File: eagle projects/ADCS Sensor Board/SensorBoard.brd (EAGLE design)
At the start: 91 x 91 mm, 96 parts, among them J1 HDR_10_EZFET_DEBUGGER, J2 MTI-1_8428-11B1-RK-TP, Q1 BC850SMD, Q2 IRF7507TRPBF, U1 MSP430F5529IPN, U2 LMV321, U3 ADS7841E_2K5, U4 LMV321, U5 LMV321, Y1 32.768kHz, Y2 CSTCR4M00G15L99

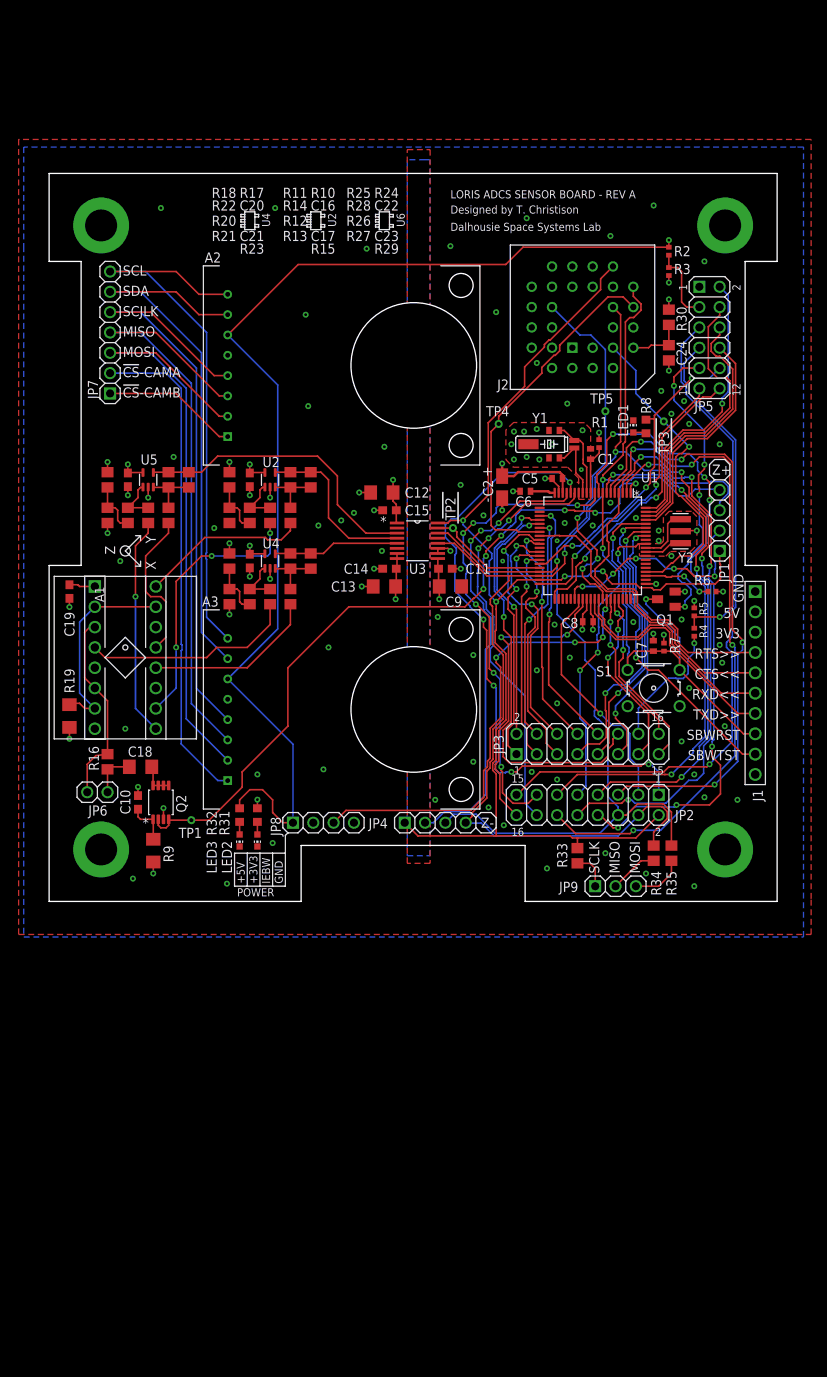
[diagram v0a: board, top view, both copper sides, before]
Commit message: Replaced obsolete transistor Q2
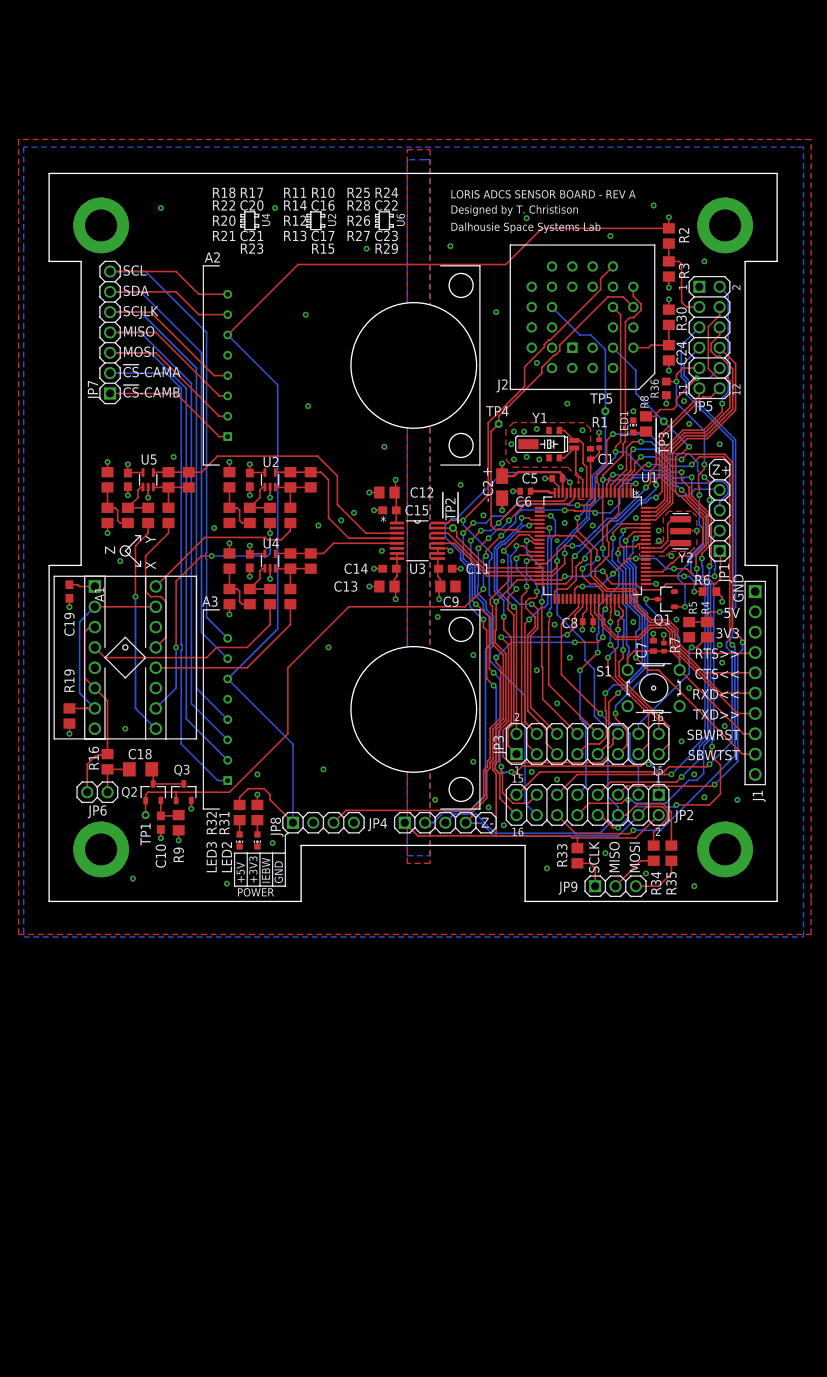
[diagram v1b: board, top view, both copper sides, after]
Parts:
- added Q3: IRLML2246TRPBF, my_library:SOT23-3P95_237X112L25X40N_MICRO3
- added R36: 10k, rcl:R0603
- C12, C13, C9: device resistor:C1206 -> rcl:C0805
- Q1: value BC850SMD -> PMV16XN; device transistor-npn:SOT23-BEC -> my_library:SOT23-3P95_230X110L20X43N_PMV16XN
- Q2: value IRF7507TRPBF -> IRLML6246TRPBF; device my_library:SOP8P65_300X490X111L53X30N -> my_library:SOT23-3P95_237X112L25X40N_MICRO3
- R19, R9: device resistor:R1206 -> rcl:R0805
- R2, R3, R4, R5: device rcl:R0402 -> rcl:R0805
- R31, R32, R8: device rcl:R0603 -> rcl:R0805
- R6: device rcl:R0402 -> rcl:R0603
- moved TP1 5.75 mm to (12.1, 10.8)
- moved R9 4.72 mm to (16.2, 9.84)
- moved C10 3.82 mm to (14.0, 9.84), turned to 90 degrees
- moved R5 2.31 mm to (80.0, 34.0), turned to 90 degrees
- moved R2 1.91 mm to (77.5, 83.2)
- moved R4 1.62 mm to (82.2, 34.0)
- moved Q2 1.59 mm to (13.0, 13.7)
- moved C12 0.63 mm to (42.2, 51.1)
- moved R3 0.32 mm to (77.5, 79.1)
- moved R6 0.32 mm to (82.5, 38.7)
- moved C13 0.32 mm to (42.2, 39.4)
- moved C9 0.32 mm to (49.8, 39.4)
- moved R31 0.32 mm to (26.0, 11.1)
- moved R32 0.32 mm to (23.8, 11.1)
- moved C18 0.32 mm to (11.4, 16.5)
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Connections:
- removed net N$38: C18.1, Q2.5, Q2.6, Q2.7, Q2.8
- new net N$9: C18.1, Q2.3, Q3.3
- net GND: now also Q1.2, Q3.2, R36.1; no longer Q1.E, Q2.3
- net HMC1053_RESET: now also Q2.1, Q3.1; no longer Q2.2, Q2.4
- net MSP_OBC_RESET: now also Q1.1, R36.2; no longer Q1.B
- net N$39: now also Q2.2; no longer Q2.1
- net RST/SBWTDIO: now also Q1.3; no longer Q1.C
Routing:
- net N$9: track 0.00 -> 6.44 mm
- net N$38: track 4.39 -> 0.00 mm
- net SEN_BRD_5V_PRESENT: track 9.63 -> 11.2 mm
- net HMC1053_RESET: track 90.5 -> 92.0 mm
- net N$39: track 5.47 -> 4.19 mm
- net MSP430_ACTIVE: track 38.5 -> 39.7 mm
- net +5V: track 141.0 -> 141.8 mm
- net GND: track 42.1 -> 41.3 mm, vias 111 -> 108

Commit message: Rev A Final-- I think
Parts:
- removed JP1, JP8: (no value), my_library:1X04
- removed JP5: (no value), my_library:2X06
- added J3: HDR_2X5_GRPB052VWQS-RC, my_library:GRPB052VWQS-RC
- added J4: (no value), my_library:1X02
- added J8, J9: (no value), my_library:1X04
- R2, R3, R31, R32, R4, R5, R8: device rcl:R0805 -> rcl:R0603
- moved S1 33.5 mm to (81.0, 59.7)
- moved R7 33.4 mm to (79.1, 65.1), turned to 0 degrees
- moved C7 32.1 mm to (79.4, 63.8), turned to 0 degrees
- moved Q1 30.0 mm to (79.7, 67.6), turned to 180 degrees
- moved R8 14.4 mm to (83.8, 70.8)
- moved LED1 13.6 mm to (83.8, 67.6), turned to 180 degrees
- moved R4 9.47 mm to (76.2, 26.7)
- moved R3 7.49 mm to (73.0, 85.1), turned to 270 degrees
- moved R5 7.47 mm to (78.4, 26.7)
- moved R36 7.13 mm to (79.7, 70.8), turned to 0 degrees
- moved R2 6.93 mm to (70.8, 85.1)
- moved R6 3.62 mm to (79.7, 36.5), turned to 90 degrees
- moved TP5 3.49 mm to (66.0, 61.3)
- moved R30 3.43 mm to (75.6, 70.2)
- moved TP3 3.42 mm to (73.7, 61.3), turned to 90 degrees
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- renumbered JP2 to J5, JP3 to J6, JP4 to J7, JP7 to J11, JP9 to J10
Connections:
- removed net RESERVED_3: JP5.6, U1.78
- removed net RESERVED_4: JP5.8, U1.77
- net !CS!_SPEED_X: now also U1.3; no longer U1.2
- net !CS!_SPEED_Y: now also U1.2; no longer U1.3
- net !CS!_SUN_Z+: now also J8.2; no longer JP1.2
- net !RST!_MTI: now also U1.80; no longer U1.64
- net +3V3: now also J3.7, J9.2; no longer JP5.1, JP8.2
- net +5V: now also J9.1; no longer JP8.1
- net ACT_BRD_3V_PRESENT: now also J3.4; no longer JP5.7
- net ACT_BRD_5V_SHIFTED: now also J3.2; no longer JP5.5
- net GND: now also J9.4; no longer JP8.4
- net INIT_EPS_BURN_WIRE: now also J9.3; no longer JP8.3
- net MSP430_ACTIVE: now also J3.10, U1.77; no longer JP5.10, U1.35
- net MSP_OBC_RESET: now also J3.5; no longer JP5.9
- net RESERVED_1: now also J3.6, U1.79; no longer JP5.2, U1.80
- net RESERVED_2: now also J3.8, U1.78; no longer JP5.4, U1.79
- net SEN_BRD_5V_PRESENT: now also J3.9; no longer JP5.3
- net UCA0RXD: now also J3.1, J4.2; no longer JP5.12
- net UCA0TXD: now also J3.3, J4.1; no longer JP5.11
- net UCB0_SPI_CLK: now also J8.1; no longer JP1.1
- net UCB0_SPI_MISO: now also J8.4; no longer JP1.4
- net UCB0_SPI_MOSI: now also J8.3; no longer JP1.3
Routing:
- net RESERVED_3: track 32.2 -> 0.00 mm
- net RESERVED_4: track 29.2 -> 0.00 mm
- net MSP_OBC_RESET: track 38.4 -> 11.9 mm, vias 4 -> 0
- net UCA0TXD: track 35.7 -> 60.0 mm, vias 2 -> 0
- net UCA0RXD: track 37.2 -> 52.5 mm, vias 2 -> 0
- net ACT_BRD_5V_SHIFTED: track 45.3 -> 60.3 mm, vias 1 -> 2
- net RST/SBWTDIO: track 57.7 -> 72.7 mm, vias 2 -> 0
- net !RST!_MTI: track 39.6 -> 24.9 mm
- net ACT_BRD_5V_PRESENT: track 16.0 -> 5.92 mm
- net SEN_BRD_5V_PRESENT: track 11.2 -> 20.9 mm
- net MSP430_ACTIVE: track 39.7 -> 30.6 mm, vias 3 -> 0
- net !COUNT_EN: track 76.5 -> 69.0 mm
- net !CS!_SPEED_Y: track 69.8 -> 63.1 mm
- net !CS!_CURRENT_SENSE_1: track 78.7 -> 72.7 mm
- net !CS!_MTI: track 44.8 -> 49.8 mm
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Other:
- board text added: "J3"
- board text added: "RX"
- board text added: "TX"
- board text removed: "5V"

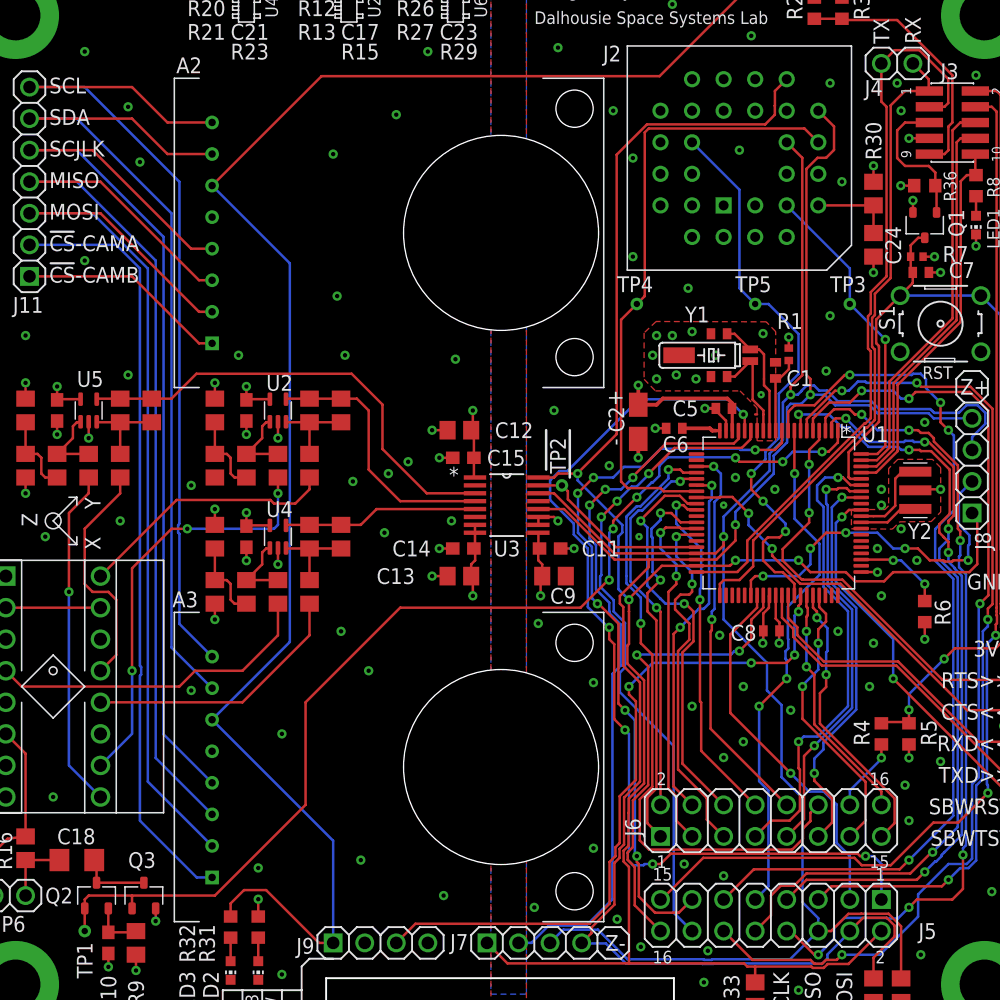
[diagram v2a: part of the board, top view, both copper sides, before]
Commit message: Added mounting holes for sun sensor board, added standoff mounting holes to sensor board
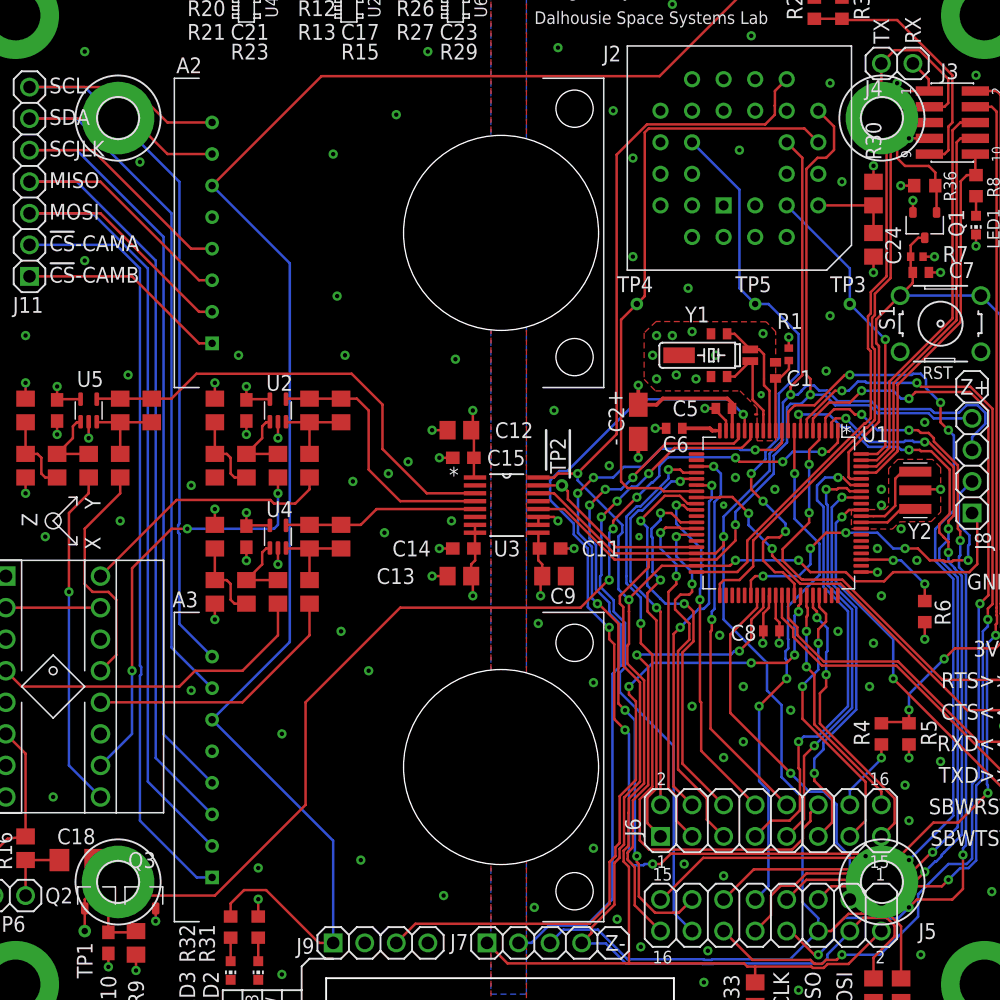
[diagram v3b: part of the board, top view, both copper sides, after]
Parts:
- added H1, H2, H3, H4: MOUNT-PAD-ROUND3.2, holes:3,2-PAD
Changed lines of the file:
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@@
 <setting verticaltext="up"/>
 </settings>
-<grid distance="12.5" unitdist="mil" unit="mil" style="lines" multiple="1" display="yes" altdistance="5" altunitdist="mil" altunit="mil"/>
+<grid distance="12.5" unitdist="mil" unit="mm" style="lines" multiple="1" display="yes" altdistance="5" altunitdist="mil" altunit="mil"/>
 <layers>
 <layer number="1" name="Top" color="4" fill="1" visible="yes" active="yes"/>
@@
 <layer number="21" name="tPlace" color="58" fill="1" visible="yes" active="yes"/>
 <layer number="22" name="bPlace" color="7" fill="1" visible="yes" active="yes"/>
-<layer number="23" name="tOrigins" color="15" fill="1" visible="no" active="yes"/>
+<layer number="23" name="tOrigins" color="15" fill="1" visible="yes" active="yes"/>
 <layer number="24" name="bOrigins" color="15" fill="1" visible="yes" active="yes"/>
 <layer number="25" name="tNames" color="7" fill="1" visible="yes" active="yes"/>
@@
 </layers>
 <board>
-<fusionsync huburn="a.YnVzaW5lc3M6bXlkYWwyMA" projecturn="a.YnVzaW5lc3M6bXlkYWwyMCMyMDE5MDkwNjIxMzMzMjg1MQ" f3durn="urn:adsk.wipprod:dm.lineage:64MLwcZoSu-ToTZFUGJpvg" pcbguid="" lastpulledtime="" lastsyncedchangeguid="" latestrevisionid="b1fc5ece-65cf-4480-81ac-8bb20170a148" lastsyncedrevisionid="b1fc5ece-65cf-4480-81ac-8bb20170a148" lastboardhashguid="72910140-9e17-6fcb-e1b4-b60b7390f1dc" lastpushedtime="2020-11-14T21:38:49Z" linktopcb3d="true"/>
+<fusionsync huburn="a.YnVzaW5lc3M6bXlkYWwyMA" projecturn="a.YnVzaW5lc3M6bXlkYWwyMCMyMDE5MDkwNjIxMzMzMjg1MQ" f3durn="urn:adsk.wipprod:dm.lineage:64MLwcZoSu-ToTZFUGJpvg" pcbguid="" lastpulledtime="" lastsyncedchangeguid="" latestrevisionid="b1fc5ece-65cf-4480-81ac-8bb20170a148" lastsyncedrevisionid="b1fc5ece-65cf-4480-81ac-8bb20170a148" lastboardhashguid="72910140-9e17-6fcb-e1b4-b60b7390f1dc" lastpushedtime="2020-11-14T21:38:49Z" linktopcb3d="false"/>
 <plain>
 <wire x1="0" y1="0" x2="31.5" y2="0" width="0.1524" layer="20"/>
@@
 </element>
 <element name="DRILEGEND" library="drilegend" package="DRILEGEND" value="" x="-4.5466" y="-8.3566" smashed="yes"/>
+<element name="H1" library="holes" library_urn="urn:adsk.eagle:library:237" package="3,2-PAD" package3d_urn="urn:adsk.eagle:package:14282/1" value="MOUNT-PAD-ROUND3.2" x="14.75" y="76.245" smashed="yes">
+<attribute name="POPULARITY" value="4" x="14.75" y="76.245" size="1.778" layer="27" display="off"/>
+</element>
+<element name="H2" library="holes" library_urn="urn:adsk.eagle:library:237" package="3,2-PAD" package3d_urn="urn:adsk.eagle:package:14282/1" value="MOUNT-PAD-ROUND3.2" x="76.245" y="76.245" locked="yes" smashed="yes">
+<attribute name="POPULARITY" value="4" x="76.245" y="76.245" locked="yes" size="1.778" layer="27" display="off"/>
+</element>
+<element name="H3" library="holes" library_urn="urn:adsk.eagle:library:237" package="3,2-PAD" package3d_urn="urn:adsk.eagle:package:14282/1" value="MOUNT-PAD-ROUND3.2" x="76.245" y="14.75" locked="yes" smashed="yes">
+<attribute name="POPULARITY" value="4" x="76.245" y="14.75" locked="yes" size="1.778" layer="27" display="off"/>
+</element>
+<element name="H4" library="holes" library_urn="urn:adsk.eagle:library:237" package="3,2-PAD" package3d_urn="urn:adsk.eagle:package:14282/1" value="MOUNT-PAD-ROUND3.2" x="14.75" y="14.75" locked="yes" smashed="yes">
+<attribute name="POPULARITY" value="4" x="14.75" y="14.75" locked="yes" size="1.778" layer="27" display="off"/>
+</element>
 </elements>
 <signals>

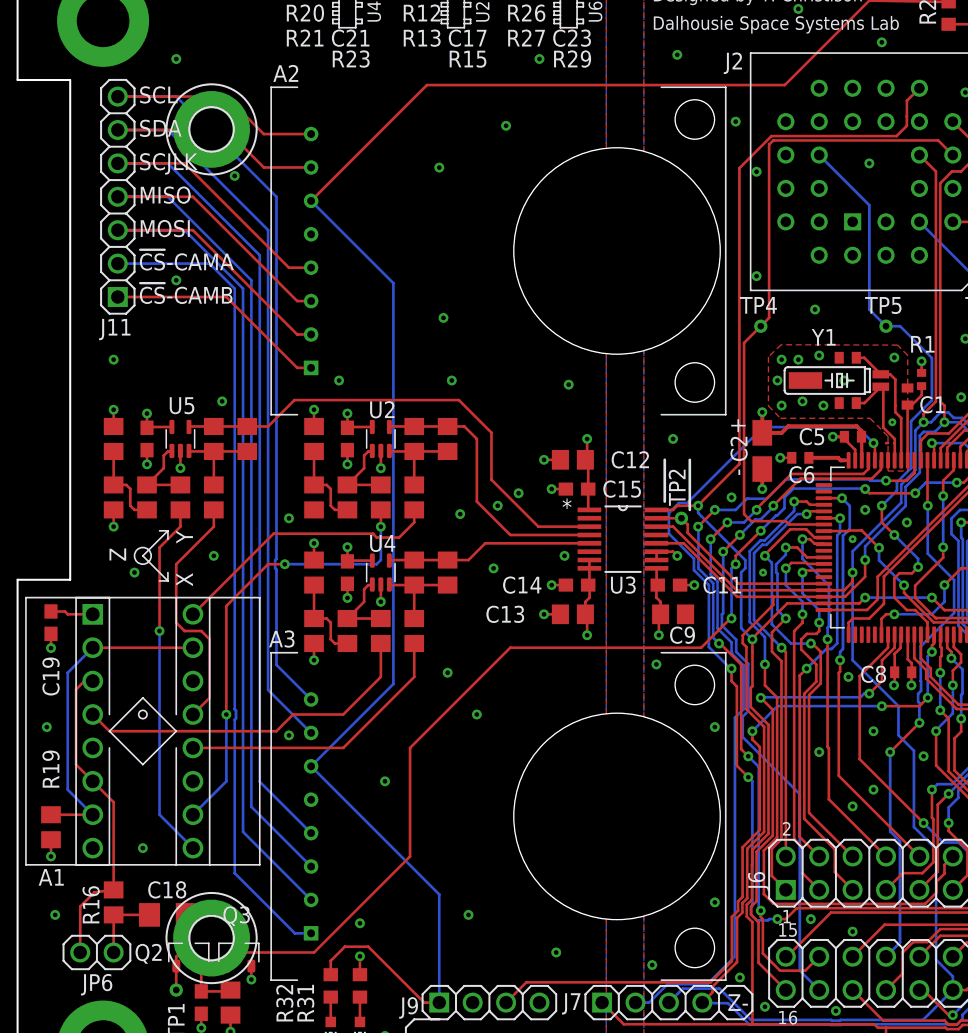
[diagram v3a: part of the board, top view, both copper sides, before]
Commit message: sensor board updates for rev b
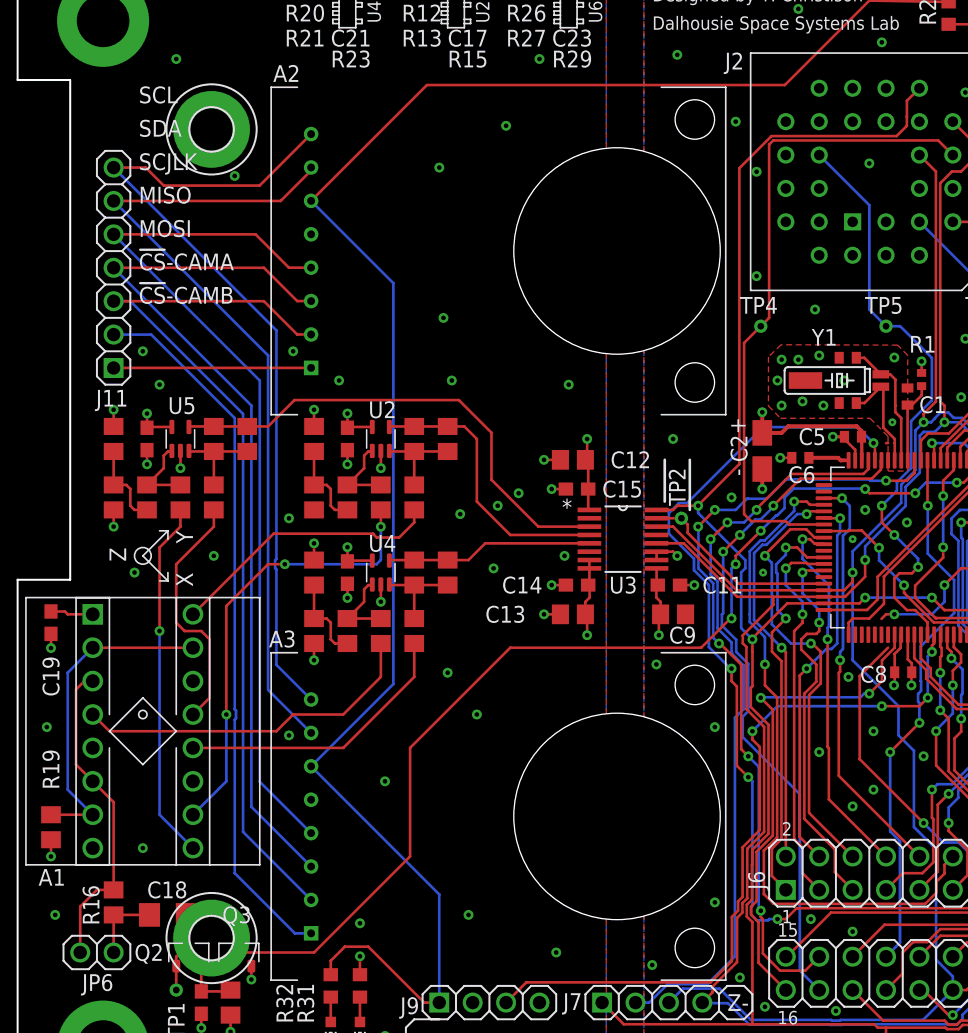
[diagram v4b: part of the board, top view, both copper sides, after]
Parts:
- moved J11 5.41 mm to (7.30, 65.7)
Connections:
- new net UCB1_I2C_SCL: U1.47
- new net UCB1_I2C_SDA: U1.46
- net !CS!_SUN_Y+: no longer U1.47
- net !CS!_SUN_Z+: no longer U1.46
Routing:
- net PAYLOAD_MOSI: track 78.0 -> 68.6 mm
- net PAYLOAD_MISO: track 77.2 -> 67.8 mm
- net PAYLOAD_SCLK: track 77.2 -> 67.8 mm
- net !CS!_CAM_B: track 61.9 -> 54.2 mm
- net PAYLOAD_SDA: track 70.1 -> 62.9 mm
- net PAYLOAD_SCL: track 70.5 -> 64.0 mm
- net !CS!_CAM_A: track 16.9 -> 15.0 mm
- net !CS!_SUN_Z+: track 29.2 -> 28.0 mm
- net !CS!_SUN_Y+: track 30.1 -> 29.1 mm
